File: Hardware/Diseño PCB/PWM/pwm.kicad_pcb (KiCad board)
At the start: 2 copper layers, 30 parts, among them Q3 BC546, U1 LM319, U2 IR2111, U3 TL082, U5 TL431LP

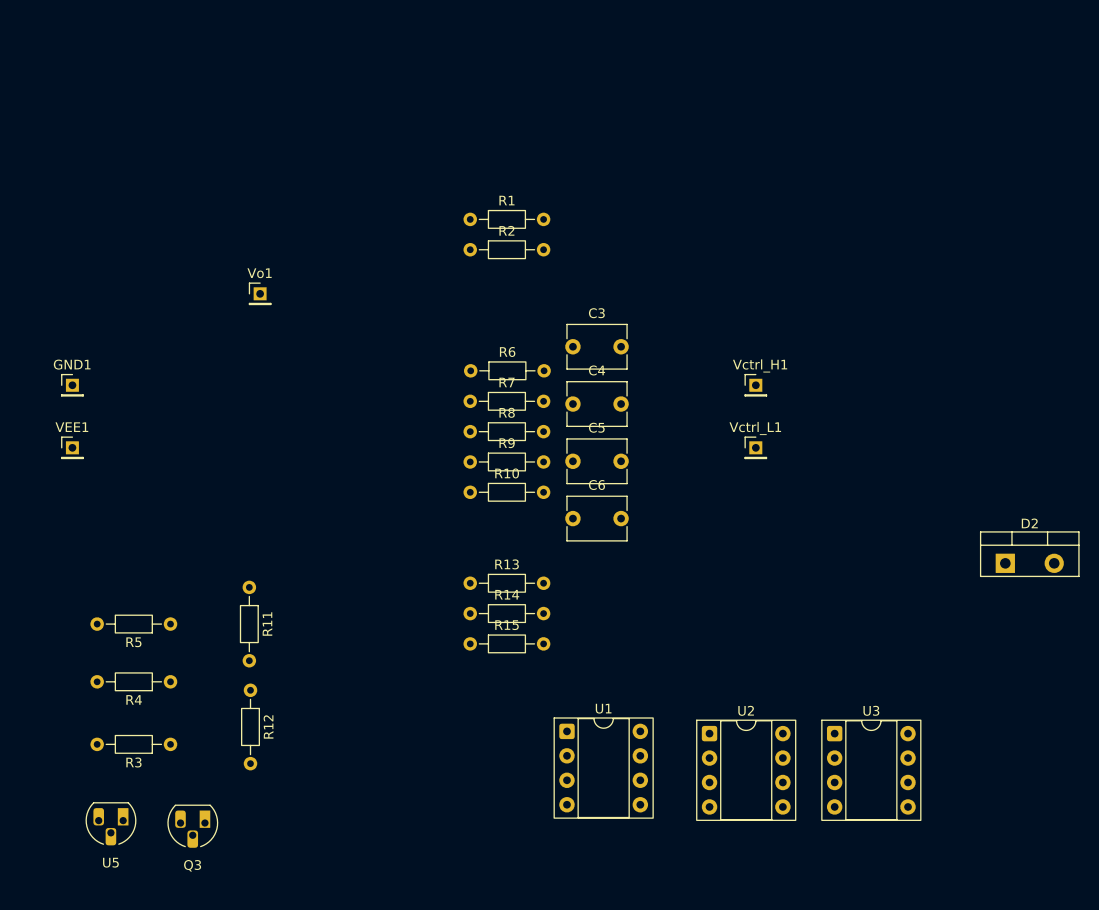
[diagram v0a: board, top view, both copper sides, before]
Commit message: CHK4: PWM esquematico en Kicad
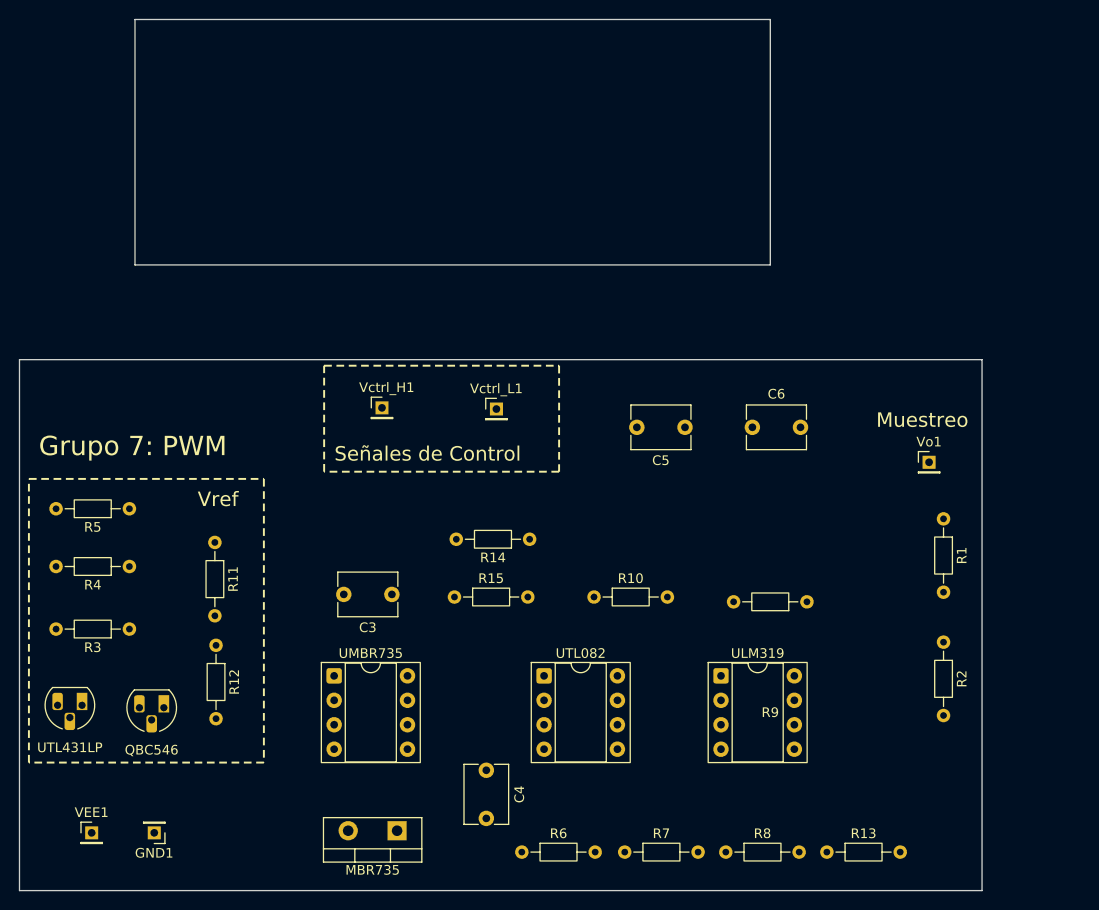
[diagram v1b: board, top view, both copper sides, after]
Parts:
- moved Vo1 71.7 mm to (184.5, 78.0)
- moved MBR735 69.0 mm to (129.2, 116.3), turned to 180 degrees
- moved R2 63.9 mm to (186.0, 96.7), turned to -90 degrees
- moved R1 58.2 mm to (186.0, 83.9), turned to -90 degrees
- moved R8 51.1 mm to (163.4, 118.5)
- moved R6 50.3 mm to (142.2, 118.5)
- moved R7 49.5 mm to (152.9, 118.5)
- moved GND1 47.3 mm to (104.0, 116.5), turned to 180 degrees
- moved R13 46.4 mm to (173.9, 118.5)
- moved VEE1 40.0 mm to (97.5, 116.5)
- moved UMBR735 39.5 mm to (122.7, 100.2)
- moved C4 39.1 mm to (138.5, 110.0), turned to -90 degrees
- moved Vctrl_H1 38.9 mm to (127.7, 72.3)
- moved R9 37.9 mm to (171.8, 92.5), turned to 180 degrees
- moved C3 31.9 mm to (128.7, 91.7), turned to 180 degrees
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- renumbered D2 to MBR735, Q3 to QBC546, U1 to ULM319, U2 to UMBR735, U3 to UTL082, U5 to UTL431LP
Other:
- board outline added: 100 x 90.5 mm
- board text added: "Grupo 7: PWM"
- board text added: "Muestreo"
- board text added: "Señales de Control"
- board text added: "Vref"

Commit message: CHK4: PWM esquematico en Kicad
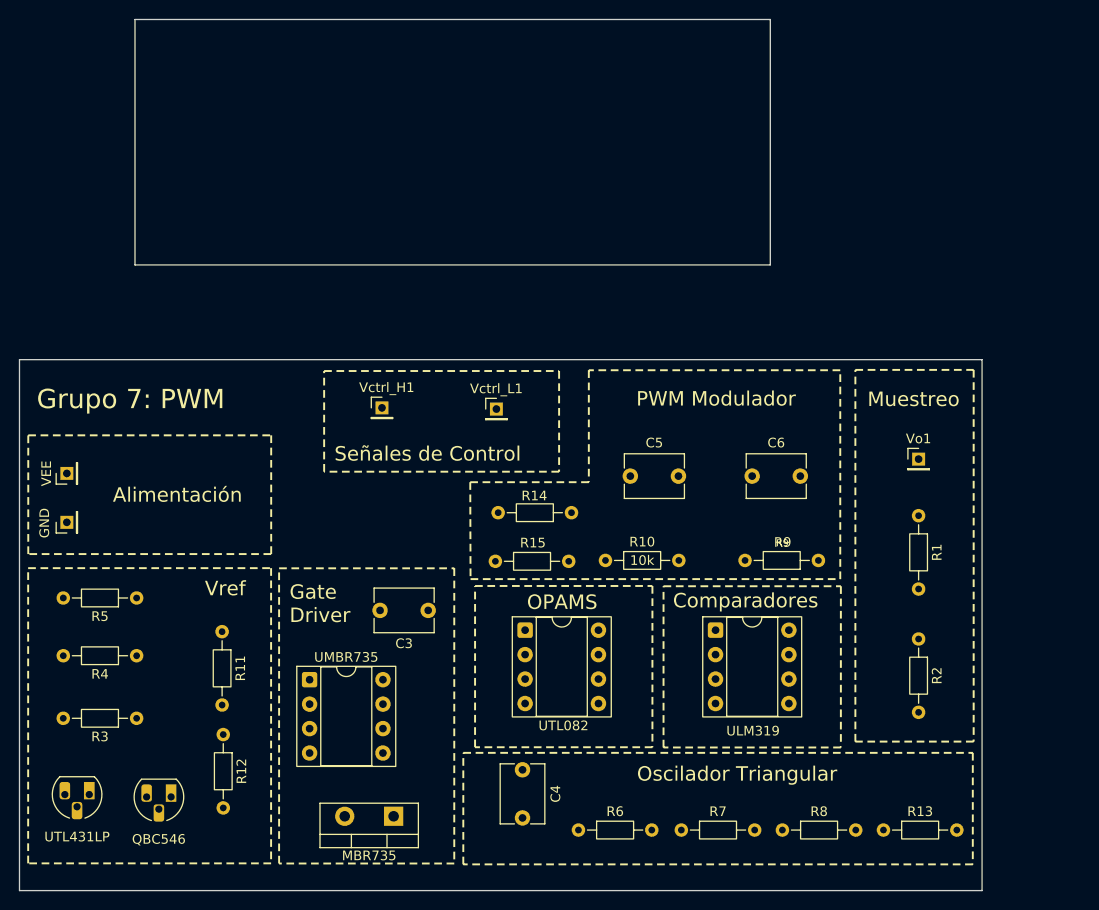
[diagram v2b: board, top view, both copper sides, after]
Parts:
- moved VEE 37.4 mm to (94.9, 79.2), turned to 90 degrees
- moved GND 33.5 mm to (94.9, 84.2), turned to 90 degrees
- moved R12 9.30 mm to (111.2, 106.3)
- moved QBC546 9.30 mm to (105.8, 112.8)
- moved R11 9.30 mm to (111.0, 95.6)
- moved R3 9.30 mm to (102.2, 104.6)
- moved R4 9.30 mm to (102.2, 98.1)
- moved R5 9.30 mm to (102.2, 92.1)
- moved UTL431LP 9.30 mm to (97.2, 112.5)
- moved C5 7.61 mm to (153.5, 79.4), turned to 0 degrees
- moved R13 6.31 mm to (179.8, 116.2)
- moved R6 6.31 mm to (148.1, 116.2)
- moved R7 6.31 mm to (158.8, 116.2)
- moved R8 6.31 mm to (169.3, 116.2)
- moved R15 5.64 mm to (139.4, 88.3)
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- renumbered GND1 to GND, VEE1 to VEE
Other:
- board text added: "Alimentación"
- board text added: "Comparadores"
- board text added: "Gate Driver"
- board text added: "OPAMS"
- board text added: "Oscilador Triangular"
- board text added: "PWM Modulador"

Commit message: CHK4: PWM esquematico en Kicad
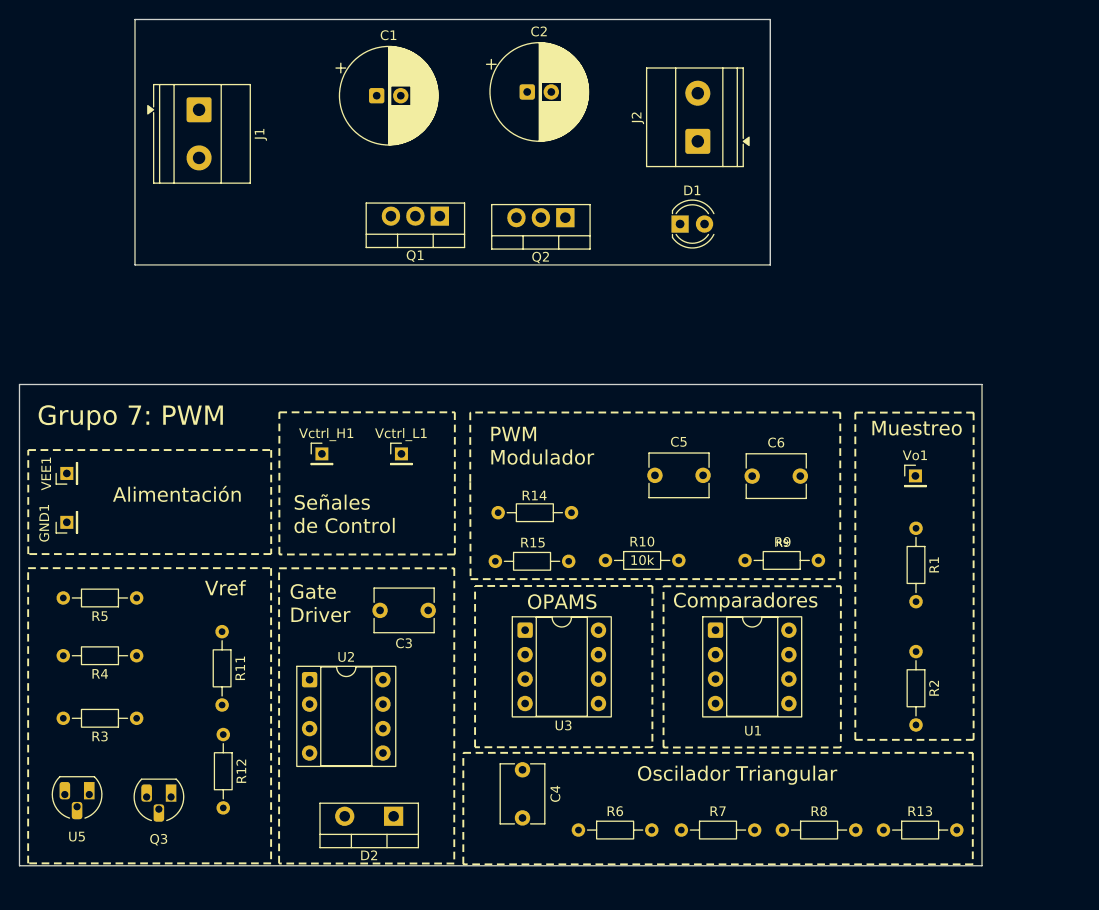
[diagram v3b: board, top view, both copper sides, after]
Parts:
- added C1: 100u, Capacitor_THT:CP_Radial_D10.0mm_P2.50mm, F.Cu at (127.1, 39.9)
- added C2: 100u, Capacitor_THT:CP_Radial_D10.0mm_P2.50mm, F.Cu at (142.8, 39.5)
- added D1: LED, LED_THT:LED_D4.0mm, F.Cu at (158.6, 53.2)
- added J1: VE, TerminalBlock_Phoenix:TerminalBlock_Phoenix_MKDS-1,5-2_1x02_P5.00mm_Horizontal, F.Cu at (108.7, 41.4)
- added J2: Vo, TerminalBlock_Phoenix:TerminalBlock_Phoenix_MKDS-1,5-2_1x02_P5.00mm_Horizontal, F.Cu at (160.5, 44.7)
- added Q1: NMOS, Package_TO_SOT_THT:TO-220-3_Vertical, F.Cu at (133.7, 52.4)
- added Q2: NMOS, Package_TO_SOT_THT:TO-220-3_Vertical, F.Cu at (146.7, 52.6)
- moved Vctrl_L1 10.9 mm to (129.7, 77.1)
- moved Vctrl_H1 7.86 mm to (121.4, 77.1)
- moved C5 2.56 mm to (156.0, 79.4)
- moved Vo1 1.78 mm to (183.1, 79.4)
- moved R1 1.34 mm to (183.1, 84.9)
- moved R2 1.34 mm to (183.1, 97.7)
- renumbered MBR735 to D2, GND to GND1, QBC546 to Q3, ULM319 to U1, UMBR735 to U2, UTL082 to U3, UTL431LP to U5, VEE to VEE1
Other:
- board size 100 x 90.5 mm -> 100 x 87.9 mm

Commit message: CHK4: PWM esquematico en Kicad
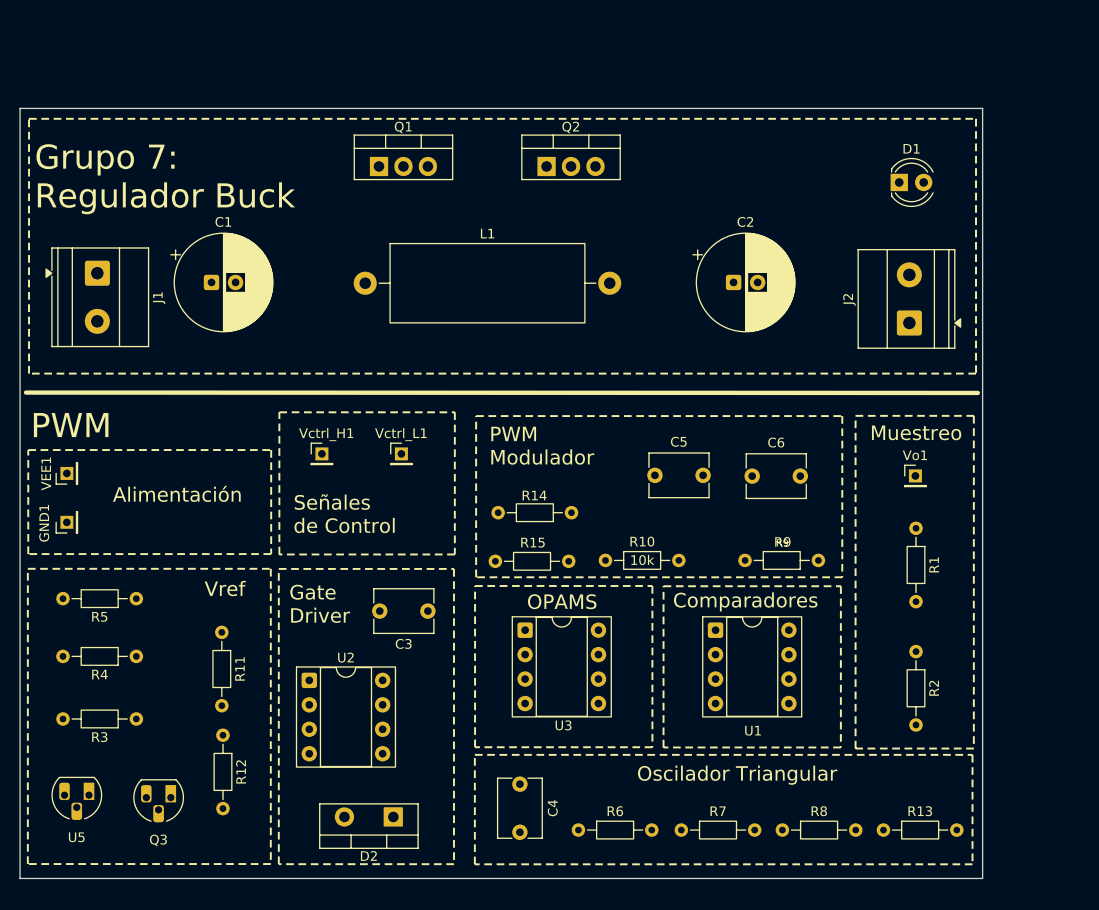
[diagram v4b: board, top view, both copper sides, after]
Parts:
- added L1: 50u, Inductor_THT:L_Axial_L20.0mm_D8.0mm_P25.40mm_Horizontal, F.Cu at (125.9, 59.4)
- moved C2 29.2 mm to (164.2, 59.3)
- moved J2 29.0 mm to (182.4, 63.5)
- moved C1 25.9 mm to (110.0, 59.3)
- moved D1 23.2 mm to (181.4, 48.9)
- moved J1 20.0 mm to (98.1, 58.4)
- moved Q1 8.16 mm to (127.3, 47.3), turned to 0 degrees
- moved Q2 5.67 mm to (144.8, 47.3), turned to 0 degrees
- moved C4 1.51 mm to (142.0, 111.4)
- moved Q3 0.08 mm to (105.7, 112.8)
- moved R11 0.08 mm to (111.0, 95.7)
- moved R3 0.08 mm to (102.1, 104.7)
- moved R4 0.08 mm to (102.1, 98.2)
- moved R5 0.08 mm to (102.1, 92.2)
- moved U5 0.08 mm to (97.2, 112.6)
- moved C3 0.08 mm to (132.4, 93.5)
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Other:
- board size 100 x 87.9 mm -> 100 x 80 mm
- board text added: "Grupo 7: Regulador Buck"
- board text added: "PWM"
- board text removed: "Grupo 7: PWM"

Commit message: CHK4:
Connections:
- C2 pad 1: Net-(D1-A) -> /Vo
- D1 pad 2: Net-(D1-A) -> /Vo
- J2 pad 2: Net-(D1-A) -> /Vo
- L1 pad 2: Net-(D1-A) -> /Vo
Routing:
- net /VEE: track 0.00 -> 105.6 mm
- net GND: track 0.00 -> 74.0 mm
- net /Vctrl_H: track 0.00 -> 48.6 mm
- net /Vctrl_L: track 0.00 -> 40.1 mm
- net /Vo: track 0.00 -> 33.4 mm
- net Net-(D2-K): track 0.00 -> 29.0 mm
- net Net-(U5-REF): track 0.00 -> 25.6 mm
- net Net-(U1A-+): track 0.00 -> 17.7 mm
- net Net-(U3B--): track 0.00 -> 16.8 mm
- net /Vcc5: track 0.00 -> 16.2 mm
- net Net-(Q3-B): track 0.00 -> 7.99 mm
- net /V_triag: track 0.00 -> 6.18 mm
- net /v_muestra: track 0.00 -> 5.19 mm
- net /Vmed: track 0.00 -> 3.12 mm
- net /V_cuad: track 0.00 -> 2.88 mm

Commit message: CHK4: PCB pistas
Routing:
- net /PWM: track 0.00 -> 174.0 mm
- net /VEE: track 105.6 -> 220.3 mm
- net /Vcc5: track 16.2 -> 129.5 mm
- net /Vmed: track 3.12 -> 96.0 mm
- net /Vo: track 33.4 -> 113.7 mm
- net GND: track 74.0 -> 152.4 mm
- net /Vctrl_L: track 40.1 -> 103.4 mm
- net Net-(U3A--): track 0.00 -> 53.7 mm
- net /v_muestra: track 5.19 -> 53.4 mm
- net Net-(U3B--): track 16.8 -> 64.8 mm
- net /Vctrl_H: track 48.6 -> 86.9 mm
- net Net-(U1B-+): track 0.00 -> 33.9 mm
- net Net-(Q1-S): track 0.00 -> 27.2 mm
- net Net-(C6-Pad1): track 0.00 -> 22.8 mm
- net Net-(Q3-B): track 7.99 -> 30.5 mm
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- added copper zone on B.Cu, net GND

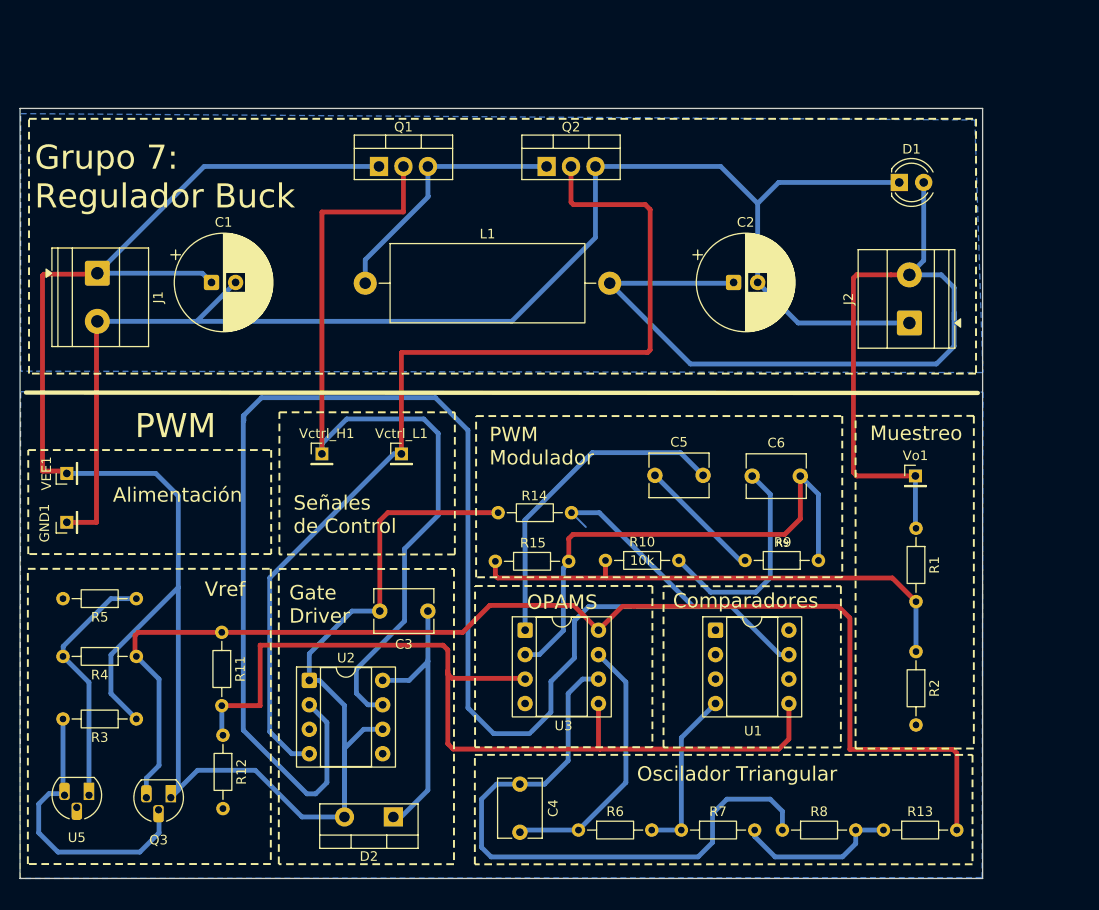
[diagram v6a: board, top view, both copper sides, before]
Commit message: CHK4: Correccion pcb NMOS
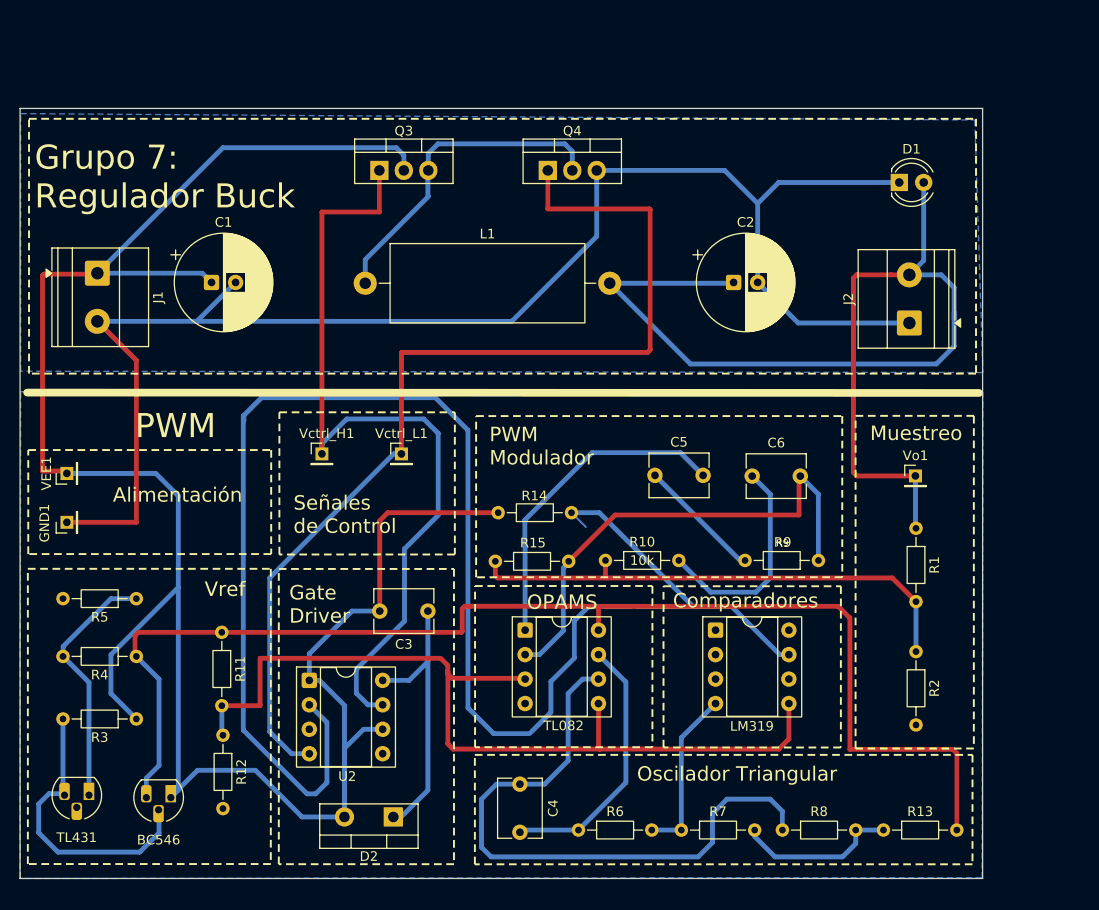
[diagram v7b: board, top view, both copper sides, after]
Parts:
- removed Q1, Q2: NMOS, Package_TO_SOT_THT:TO-220-3_Vertical
- added Q3: IRF540N, Package_TO_SOT_THT:TO-220-3_Vertical, F.Cu at (127.4, 47.7)
- added Q4: IRF540N, Package_TO_SOT_THT:TO-220-3_Vertical, F.Cu at (144.9, 47.7)
- renumbered Q3 to BC546, U1 to LM319, U3 to TL082, U5 to TL431
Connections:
- LM319 pad 6: GND -> (no net)
- TL082 pad 4: GND -> (no net)
- TL082 pad 8: /Vcc5 -> (no net)
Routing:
- net Net-(Q3-S): track 27.2 -> 34.3 mm
- net /VEE: track 220.3 -> 225.6 mm
- net GND: track 152.4 -> 157.6 mm
- net /Vmed: track 96.0 -> 93.0 mm
- net /Vctrl_H: track 86.9 -> 84.0 mm
- net /Vctrl_L: track 103.4 -> 105.8 mm
- net /Vcc5: track 129.5 -> 131.3 mm
- net Net-(TL082A--): track 53.7 -> 52.0 mm
